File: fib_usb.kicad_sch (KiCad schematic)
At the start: 139 parts, among them J401 USB-C_USB4105-GF-A, J402 Conn_USB-C_WE_632723300011, U3 TPS65988DHRSHR, U403 FT230X_QFN, U404 AP22615A_TSOT26, U405 TUSB1046-DCIRNQ, U406 AP22615A_TSOT26, U407 TPD4E05U06QDQARQ1, U408 TPD4E05U06QDQARQ1, U409 W25Q80DV_USON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

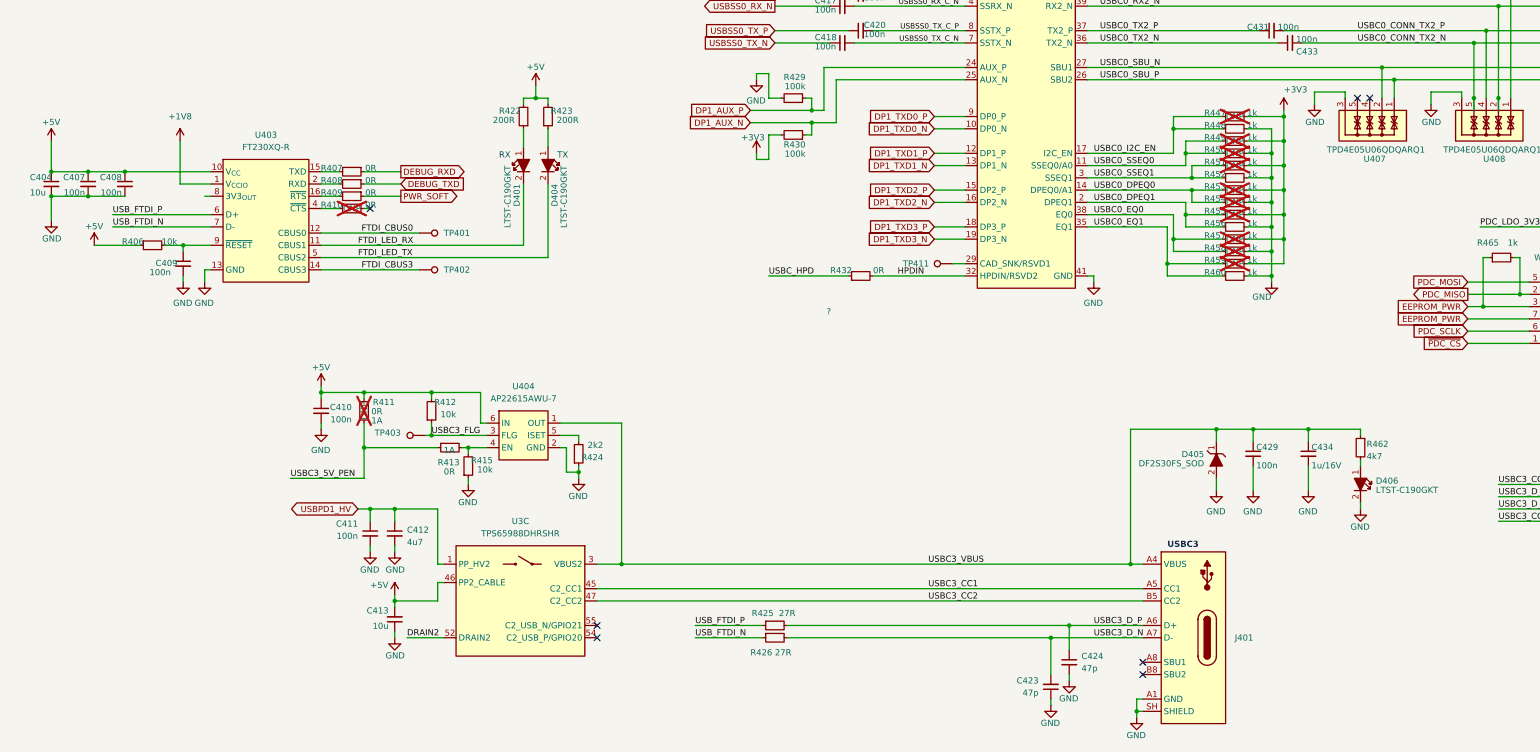
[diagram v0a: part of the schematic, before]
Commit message: replaced 1v8 buck with ldo, added startup circuit, added footprints for eink connectors
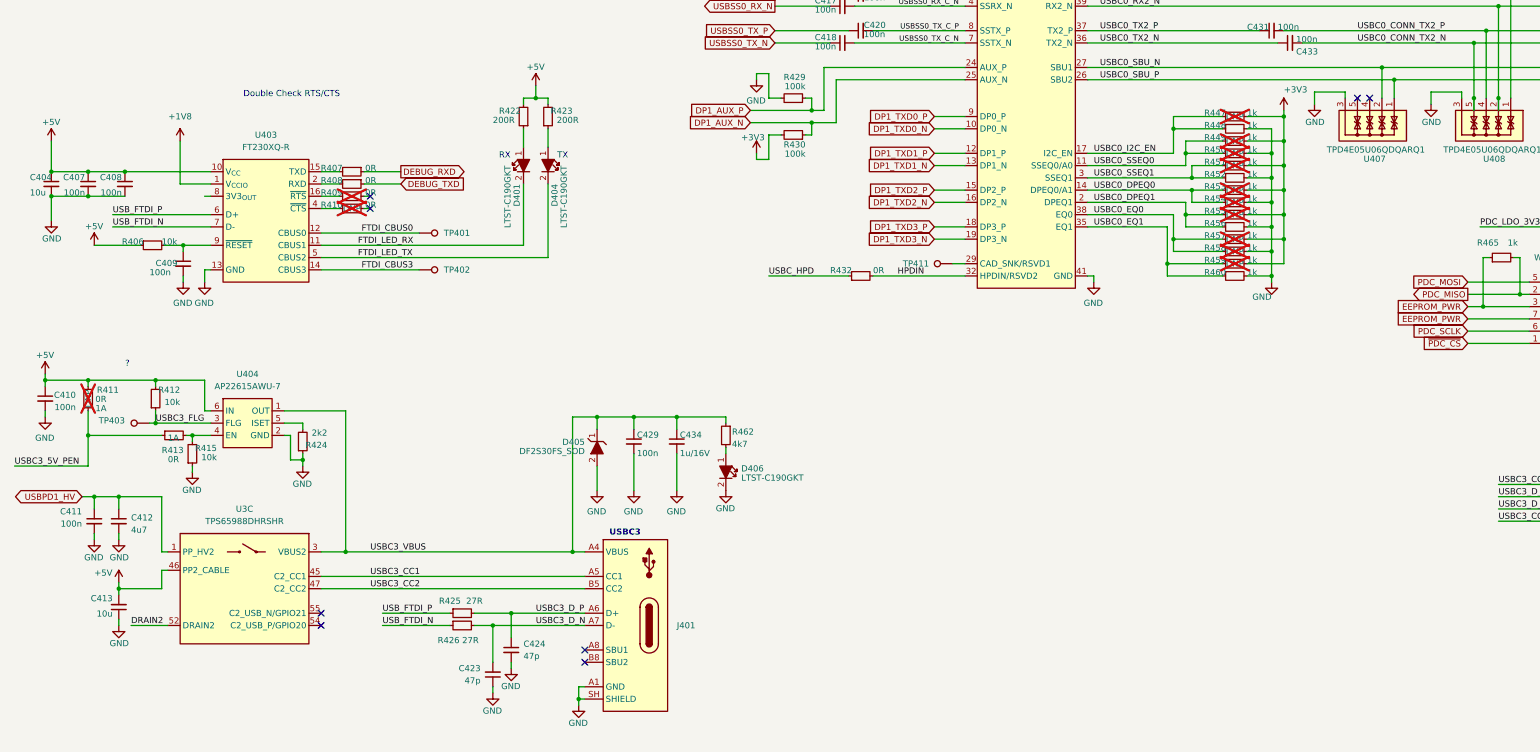
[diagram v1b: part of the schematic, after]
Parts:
- R409: now not fitted
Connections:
- net PWR_SOFT: no longer names the net of R409.1
- no-connect marks 12 -> 13
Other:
- note added: "Double Check RTS/CTS"
- moved on the sheet: C410, C411, C412, C413, C423, C424, C429, C434, D405, D406, J401, R411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

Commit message: added all missing footprints, fixed library & footprint links, did layout out 99% of components, all that's left is rtc(?), peripherals, routing & lengthmatching and final sanity checks
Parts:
- C401, C403, C404, C405, C413, C422, C428: symbol jetson-orin-baseboard:C_10u_0402 -> Fibel2:C_Small_Rota
- C402, C407, C408, C409, C410, C411, C414, C415, C416, C417, C418, C419, C420, C421, C425, C426, C429, C430, C431, C432, C433, C435, C436: symbol jetson-orin-baseboard:C_100n_0402 -> Fibel2:C_Small_Rota
- C412, C427: symbol jetson-orin-baseboard:C_4u7_25V_0402 -> Fibel2:C_Small_Rota
- C423, C424: symbol jetson-orin-baseboard:C_47p_0402 -> Fibel2:C_Small_Rota
- C434, C437: symbol jetson-orin-baseboard:C_1u_16V_0402 -> Fibel2:C_Small_Rota
- D401, D402, D403, D404, D406, D409: symbol jetson-orin-baseboard:LED_G_0603_LTST-C190GKT -> Fibel2:LED_G_0603_LTST-C190GKT
- D405, D408: symbol jetson-orin-baseboard:DF2S30FS_SOD -> Fibel2:DF2S30FS_SOD
- D407: footprint Diode_SMD:D_SOD-523 -> Fibel2:RB521S30T1G; symbol jetson-orin-baseboard:RB521S30T1G -> Fibel2:RB521S30T1G; Availability (none) -> In Stock; Check_prices (none) -> https://www.snapeda.com/parts/BAT54WT-7/Diodes+Inc./view-pa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; Description_1 (none) -> Diodes Inc BAT54WT-7, SMT Schottky Diode, 30V 200mA, 5ns, 2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; MANUFACTURER (none) -> DIODES; MAXIMUM_PACKAGE_HEIGHT (none) -> 0.65mm; MF (none) -> Diodes Inc.; MP (none) -> BAT54WT-7; PARTREV (none) -> 3-2; Package (none) -> SOD-523 Diodes Inc.; Price (none) -> None; Purchase-URL (none) -> https://www.snapeda.com/api/url_track_click_mouser/?unipart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; STANDARD (none) -> IPC-7351B; SnapEDA_Link (none) -> https://www.snapeda.com/parts/BAT54WT-7/Diodes+Inc./view-pa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
- R401, R403, R406, R412, R415, R443, R446: symbol jetson-orin-baseboard:R_10k_0402 -> Fibel2:R_Small_Rota
- R402, R404, R429, R430: symbol jetson-orin-baseboard:R_100k_0402 -> Fibel2:R_Small_Rota
- R405, R407, R408, R409, R410, R411, R413, R416, R419, R420, R421, R432, R440, R441, R444, R445: symbol jetson-orin-baseboard:R_0R_0402 -> Fibel2:R_Small_Rota
- R417, R418, R422, R423: symbol jetson-orin-baseboard:R_200R_0402 -> Fibel2:R_Small_Rota
- R424, R461: symbol jetson-orin-baseboard:R_2k2_0402 -> Fibel2:R_Small_Rota
- R425, R426: symbol jetson-orin-baseboard:R_27R_0402 -> Fibel2:R_Small_Rota
- R435, R436, R437, R438, R462, R475: symbol jetson-orin-baseboard:R_4k7_0402 -> Fibel2:R_Small_Rota
- R447, R448, R449, R450, R451, R452, R453, R454, R455, R456, R457, R458, R459, R460, R465: symbol jetson-orin-baseboard:R_1k_0402 -> Fibel2:R_Small_Rota
- R473, R474: symbol jetson-orin-baseboard:R_2M_0402 -> Fibel2:R_Small_Rota
- TP401, TP402, TP403, TP404, TP405, TP406, TP407, TP408, TP409, TP410, TP411: value TP_0.75mm_SMD -> TestPoint; symbol jetson-orin-baseboard:TP_0.75mm_SMD -> Fibel2:TestPoint
- U403: symbol jetson-orin-baseboard:FT230X_QFN -> Fibel2:FT230X_QFN
- U404, U406: value AP22615A_TSOT26 -> AP22615_1; symbol jetson-orin-baseboard:AP22615A_TSOT26 -> Fibel2:AP22615_1; Manufacturer Diodes Incorporated -> DIODES
- U405: symbol jetson-orin-baseboard:TUSB1046-DCIRNQ -> Fibel2:TUSB1046-DCIRNQ; VSD_Class (none) -> USB-DP switch
- U407, U408, U410, U411, U412: symbol jetson-orin-baseboard:TPD4E05U06QDQARQ1 -> Fibel2:TPD4E05U06QDQARQ1
- U409: symbol jetson-orin-baseboard:W25Q80DV_USON -> Fibel2:W25Q80DV_USON
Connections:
- net PDC_I2C1_IRQn is gone; now on net PDC_I2C2_IRQn: R419.2, U3.29 (~{I2C1_IRQ})
- net PDC_I2C1_SCL is gone; now on net PDC_I2C2_SCL: R420.2, R436.2, U3.27 (I2C1_SCL)
- net PDC_I2C1_SDA is gone; now on net PDC_I2C2_SDA: R421.2, R435.2, U3.28 (I2C1_SDA)
- net EEPROM_PWR: now also D407.C; no longer D407.1
- net GND: no longer C428.2
- net GPIO010: no longer R419.1
- net PDC_LDO_3V3: now also D407.A; no longer D407.2
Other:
- moved on the sheet: C401, C403, C409, C428, R406, R440, R441, R444, R465

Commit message: did length tuning, routing of final submodules and most of power routing
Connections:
- net PDC_I2C2_IRQn: no longer R419.2, U3.29 (~{I2C1_IRQ})
- net PDC_I2C2_SCL: no longer R420.2, R436.2, U3.27 (I2C1_SCL)
- net PDC_I2C2_SDA: no longer R421.2, R435.2, U3.28 (I2C1_SDA)
- new net PDC_I2C1_IRQn: R419.2, U3.29 (~{I2C1_IRQ})
- new net PDC_I2C1_SCL: R420.2, R436.2, U3.27 (I2C1_SCL)
- new net PDC_I2C1_SDA: R421.2, R435.2, U3.28 (I2C1_SDA)
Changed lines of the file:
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@@
 		)
 	)
-	(label "PDC_I2C2_SDA"
+	(label "PDC_I2C1_SDA"
 		(at 173.355 44.45 0)
 		(fields_autoplaced yes)
@@
 		)
 	)
-	(label "PDC_I2C2_SDA"
+	(label "PDC_I2C1_SDA"
 		(at 93.98 87.63 0)
 		(fields_autoplaced yes)
@@
 		)
 	)
-	(label "PDC_I2C2_SCL"
+	(label "PDC_I2C1_SCL"
 		(at 173.355 46.99 0)
 		(fields_autoplaced yes)
@@
 		)
 	)
-	(label "PDC_I2C2_IRQn"
+	(label "PDC_I2C1_IRQn"
 		(at 93.98 82.55 0)
 		(fields_autoplaced yes)
@@
 		)
 	)
-	(label "PDC_I2C2_SCL"
+	(label "PDC_I2C1_SCL"
 		(at 93.98 85.09 0)
 		(fields_autoplaced yes)

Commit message: routed epd displays, added testpoints and all the little checks and fixe, (regrettably) removed the i80 connector, 99% there, need to double check some things add peripheral connectors, shared-ish storage and vias vias vias
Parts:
- removed R437, R438: 4.7K, Resistor_SMD:R_0402_1005Metric, symbol Fibel2:R_Small_Rota
- removed TP403, TP404, TP405, TP406, TP407, TP408, TP409, TP411: TestPoint, TestPoint:TestPoint_Pad_D1.0mm, symbol Fibel2:TestPoint
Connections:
- net GPIO010: now also R419.1
- net PDC_I2C2_IRQn: no longer names the net of U3.34 (~{I2C2_IRQ})
- net PDC_I2C2_SCL: no longer names the net of U3.32 (I2C2_SCL)
- net PDC_I2C2_SDA: no longer names the net of U3.33 (I2C2_SDA)
- net PDC_I2C3_SCL: no longer names the net of U3.21 (I2C3_SCL/GPIO5)
- net PDC_I2C3_SDA: no longer names the net of U3.22 (I2C3_SDA/GPIO6)
- net ~{PDC_I2C3_IRQ}: no longer names the net of U3.23 (~{I2C3_IRQ}/GPIO7)
- no-connect marks 13 -> 19

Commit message: adde testpoints, fixed power supplies, ready to order
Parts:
- added TPCCT0, TPCCT1, TPCF1, TPPDCS1, TPRXD1, TPSMI1, TPSMO1, TPSSC1, TPTXD1: TestPoint, TestPoint:TestPoint_Pad_D1.0mm, symbol Fibel2:TestPoint
- renumbered TP401 to TPCB0, TP402 to TPCB3, TP410 to TPHPD1
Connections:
- net DEBUG_RXD: now also TPRXD1.1
- net DEBUG_TXD: now also TPTXD1.1
- net PDC_MISO: now also TPSMI1.1
- net PDC_MOSI: now also TPSMO1.1
- net PDC_SCLK: now also TPSSC1.1
- net USBC0_CTL0: now also TPCCT0.1
- net USBC0_CTL1: now also TPCCT1.1
- net USBC0_FLIP: now also TPCF1.1
- net ~{PDC_CS}: now also TPPDCS1.1
